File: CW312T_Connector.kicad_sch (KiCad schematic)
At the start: 12 parts, among them P1 PCIEx4 EDGE CONNECTOR

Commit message: updated pcb, schematic, production files
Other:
- moved on the sheet: C10, C11, C12, C13

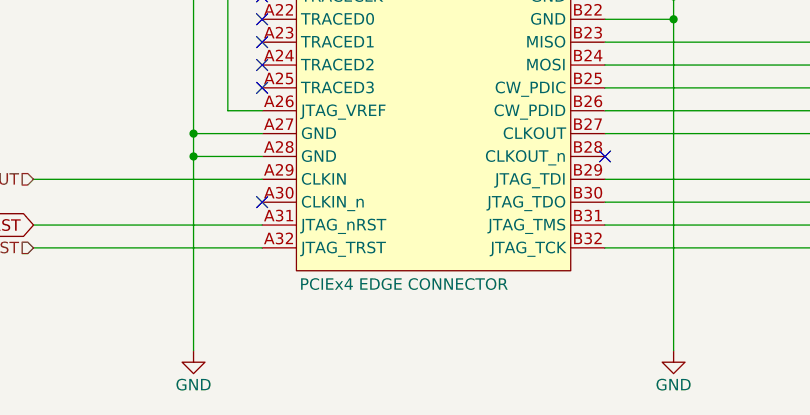
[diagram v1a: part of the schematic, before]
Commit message: updated schematic and pcb after library re-organization
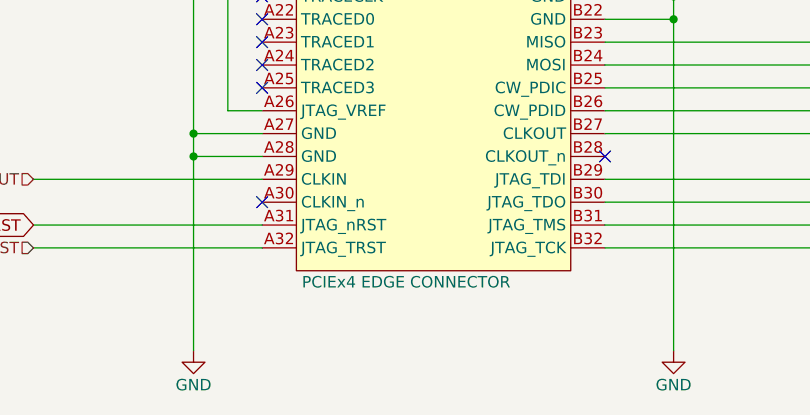
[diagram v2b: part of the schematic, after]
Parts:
- removed P1: PCIEx4 EDGE CONNECTOR, tutorial_2_library:CW312_Template, symbol tutorial_2_library:CW312T-Template
- added P1: PCIEx4 EDGE CONNECTOR, tutorial_2_library:CW312_Template, symbol NAE_Connectors:CW312T-Template
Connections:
- net +3V3: now also P1.A26 (JTAG_VREF), P1.A5 (VCC3.3), P1.B10 (IOVREF), P1.B5 (FILTIN)
- net CLK_IN: now also P1.B27 (CLKOUT)
- net CLK_OUT: now also P1.A29 (CLKIN)
- net FILT_LP: now also P1.A3 (FILT_LP), P1.B4 (FILT_HP)
- net GND: now also P1.A1 (GND), P1.A2 (GND), P1.A20 (GND), P1.A27 (GND), P1.A28 (GND), P1.A8 (GND), P1.B15 (GND), P1.B21 (GND), P1.B22 (GND), P1.B3 (GND), P1.B9 (GND)
- net J_TCK: now also P1.B32 (JTAG_TCK)
- net J_TDI: now also P1.B29 (JTAG_TDI)
- net J_TDO: now also P1.B30 (JTAG_TDO)
- net J_TMS: now also P1.B31 (JTAG_TMS)
- net J_TRST: now also P1.A32 (JTAG_TRST)
- net LED1: now also P1.B11 (LED1)
- net LED2: now also P1.B12 (LED2)
- net LED3: now also P1.B13 (LED3)
- net PG10: now also P1.A18 (HDR10)
- net PG7: now also P1.B18 (GPIO3)
- net PG9: now also P1.A17 (HDR9)
- net PH10: now also P1.A16 (HDR8)
- net PH9: now also P1.A15 (HDR7)
- net PJ10: now also P1.A14 (HDR6)
- net PJ7: now also P1.B19 (GPIO4)
- net PJ8: now also P1.A10 (HDR2)
- net PJ9: now also P1.A13 (HDR5)
- net PK10: now also P1.A12 (HDR4)
- net PK8: now also P1.A9 (HDR1)
- net PK9: now also P1.A11 (HDR3)
- net PORT_CS: now also P1.B26 (CW_PDID)
- net PORT_OE: now also P1.B25 (CW_PDIC)
- net PORT_SCK: now also P1.B20 (SCK)
- net PORT_SIO0: now also P1.B24 (MOSI)
- net PORT_SIO1: now also P1.B23 (MISO)
- net RST: now also P1.A31 (JTAG_nRST), P1.B14 (nRST)
- net SHUNTH: now also P1.B2 (SHUNTH)
- net SHUNTL: now also P1.B1 (SHUNTL)
- net UART_RX: now also P1.B17 (GPIO2/RX)
- net UART_TX: now also P1.B16 (GPIO1/TX)
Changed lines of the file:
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@@
-	)
-	(symbol
-		(lib_id "tutorial_2_library:CW312T-Template")
-		(at 81.28 53.34 0)
-		(unit 1)
-		(exclude_from_sim no)
-		(in_bom no)
-		(on_board yes)
-		(dnp no)
-		(property "Reference" "P1"
-			(at 67.056 49.784 0)
-			(effects
-				(font
-					(size 1.27 1.27)
-				)
-			)
-		)
-		(property "Value" "PCIEx4 EDGE CONNECTOR"
-			(at 77.978 136.144 0)
-			(effects
-				(font
-					(size 1.27 1.27)
-				)
-			)
-		)
-		(property "Footprint" "tutorial_2_library:CW312_Template"
-			(at 77.47 146.05 0)
-			(effects
-				(font
-					(size 1.27 1.27)
-				)
-				(hide yes)
-			)
-		)
-		(property "Datasheet" ""
-			(at 78.74 52.07 0)
-			(effects
-				(font
-					(size 1.27 1.27)
-				)
-				(hide yes)
-			)
-		)
-		(property "Description" "BOARD AND EDGE CONNECTOR TEMPLATE FOR CW312 TARGETS"
-			(at 90.17 142.24 0)
-			(effects
-				(font
-					(size 1.27 1.27)
-				)
-				(hide yes)
-			)
-		)
-		(pin "A9"
-		)
-		(pin "A2"
-		)
-		(pin "A16"
-		)
-		(pin "A29"
-		)
-		(pin "A5"
-		)
-		(pin "B17"
-		)
-		(pin "A19"
-		)
-		(pin "A31"
-		)
-		(pin "A3"
-		)
-		(pin "B21"
-		)
-		(pin "B25"
-		)
-		(pin "B31"
-		)
-		(pin "A10"
-		)
-		(pin "A14"
-		)
-		(pin "A23"
-		)
-		(pin "A26"
-		)
-		(pin "A30"
-		)
-		(pin "B4"
-		)
-		(pin "A12"
-		)
-		(pin "B5"
-		)
-		(pin "A27"
-		)
-		(pin "B24"
-		)
-		(pin "A20"
-		)
-		(pin "A22"
-		)
-		(pin "B32"
-		)
-		(pin "B6"
-		)
-		(pin "B7"
-		)
-		(pin "B8"
-		)
-		(pin "A15"
-		)
-		(pin "A18"
-		)
-		(pin "A6"
-		)
-		(pin "A1"
-		)
-		(pin "B10"
-		)
-		(pin "B2"
-		)
-		(pin "A28"
-		)
-		(pin "B1"
-		)
-		(pin "A11"
-		)
-		(pin "A4"
-		)
-		(pin "B12"
-		)
-		(pin "A32"
-		)
-		(pin "B15"
-		)
-		(pin "B20"
-		)
-		(pin "B23"
-		)
-		(pin "A21"
-		)
-		(pin "B28"
-		)
-		(pin "A7"
-		)
-		(pin "B13"
-		)
-		(pin "B29"
-		)
-		(pin "B26"
-		)
-		(pin "B30"
-		)
-		(pin "A17"
-		)
-		(pin "A13"
-		)
-		(pin "B14"
-		)
-		(pin "B27"
-		)
-		(pin "B18"
-		)
-		(pin "B19"
-		)
-		(pin "B11"
-		)
-		(pin "B22"
-		)
-		(pin "B3"
-		)
-		(pin "B16"
-		)
-		(pin "A24"
-		)
-		(pin "A8"
-		)
-		(pin "A25"
-		)
-		(pin "B9"
-		)
-		(instances
-			(project ""
-				(path "/33bbe691-2691-4fff-bd3a-7534709d61ac/7eebb7ca-1d6c-4fe4-b599-43b6ba5026a3"
-					(reference "P1")
-					(unit 1)
-				)
-			)
-		)
 	)
 	(symbol
@@
 					(unit 1)
 				)
+			)
+		)
+	)
+	(symbol
+		(lib_id "NAE_Connectors:CW312T-Template")
+		(at 81.28 53.34 0)
+		(unit 1)
+		(exclude_from_sim no)
+		(in_bom no)
+		(on_board yes)
+		(dnp no)
+		(property "Reference" "P1"
+			(at 67.056 49.784 0)
+			(effects
+				(font
+					(size 1.27 1.27)
+				)
+			)
+		)
+		(property "Value" "PCIEx4 EDGE CONNECTOR"
+			(at 78.232 135.89 0)
+			(effects
+				(font
+					(size 1.27 1.27)
+				)
+			)
+		)
+		(property "Footprint" "tutorial_2_library:CW312_Template"
+			(at 77.47 146.05 0)
+			(effects
+				(font
+					(size 1.27 1.27)
+				)
+				(hide yes)
+			)
+		)
+		(property "Datasheet" ""
+			(at 78.74 52.07 0)
+			(effects
+				(font
+					(size 1.27 1.27)
+				)
+				(hide yes)
+			)
+		)
+		(property "Description" "BOARD AND EDGE CONNECTOR TEMPLATE FOR CW312 TARGETS"
+			(at 90.17 142.24 0)
+			(effects
+				(font
+					(size 1.27 1.27)
+				)
+				(hide yes)
+			)
+		)
+		(pin "B16"
+		)
+		(pin "A14"
+		)
+		(pin "B26"
+		)
+		(pin "A25"
+		)
+		(pin "B28"
+		)
+		(pin "A13"
+		)
+		(pin "B14"
+		)
+		(pin "B25"
+		)
+		(pin "B20"
+		)
+		(pin "B29"
+		)
+		(pin "B5"
+		)
+		(pin "A27"
+		)
+		(pin "A23"
+		)
+		(pin "B18"
+		)
+		(pin "B30"
+		)
+		(pin "B6"
+		)
+		(pin "A2"
+		)
+		(pin "B7"
+		)
+		(pin "B8"
+		)
+		(pin "A21"
+		)
+		(pin "A17"
+		)
+		(pin "A22"
+		)
+		(pin "A26"
+		)
+		(pin "A1"
+		)
+		(pin "A5"
+		)
+		(pin "B1"
+		)
+		(pin "B17"
+		)
+		(pin "B10"
+		)
+		(pin "B21"
+		)
+		(pin "A10"
+		)
+		(pin "B19"
+		)
+		(pin "B13"
+		)
+		(pin "A16"
+		)
+		(pin "B11"
+		)
+		(pin "B22"
+		)
+		(pin "B24"
+		)
+		(pin "B27"
+		)
+		(pin "A18"
+		)
+		(pin "A4"
+		)
+		(pin "A6"
+		)
+		(pin "B12"
+		)
+		(pin "B2"
+		)
+		(pin "B32"
+		)
+		(pin "A11"
+		)
+		(pin "A24"
+		)
+		(pin "A8"
+		)
+		(pin "B23"
+		)
+		(pin "B3"
+		)
+		(pin "A29"
+		)
+		(pin "A28"
+		)
+		(pin "A3"
+		)
+		(pin "B31"
+		)
+		(pin "A7"
+		)
+		(pin "B4"
+		)
+		(pin "A15"
+		)
+		(pin "A9"
+		)
+		(pin "A20"
+		)
+		(pin "A32"
+		)
+		(pin "A30"
+		)
+		(pin "A19"
+		)
+		(pin "A12"
+		)
+		(pin "A31"
+		)
+		(pin "B15"
+		)
+		(pin "B9"
+		)
+		(instances
+			(project ""
+				(path "/33bbe691-2691-4fff-bd3a-7534709d61ac/7eebb7ca-1d6c-4fe4-b599-43b6ba5026a3"
+					(reference "P1")
+					(unit 1)
+				)
